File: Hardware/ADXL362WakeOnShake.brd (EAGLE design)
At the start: 43.2 x 24.1 mm, 25 parts, among them J1 PROG_HDR, U1 ADXL362, U3 ADP160-3.3

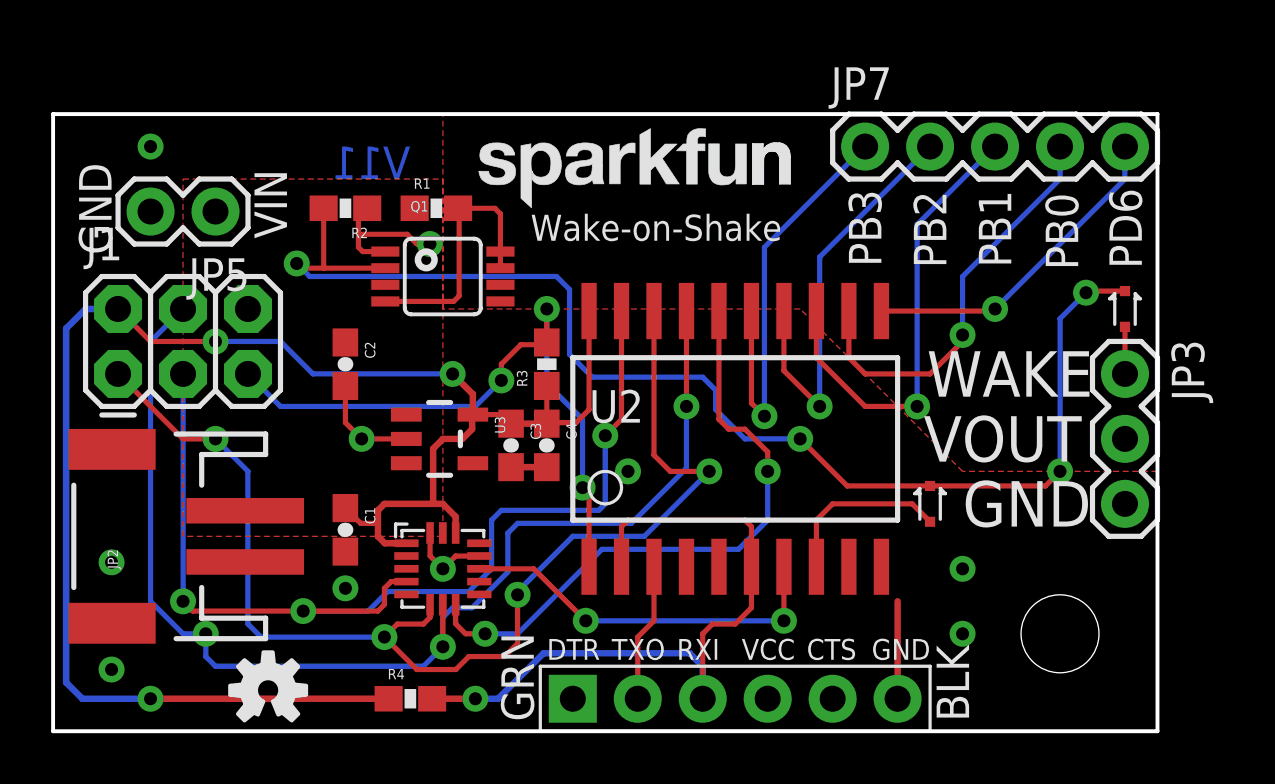
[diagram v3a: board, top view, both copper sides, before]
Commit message: added regular fiducials
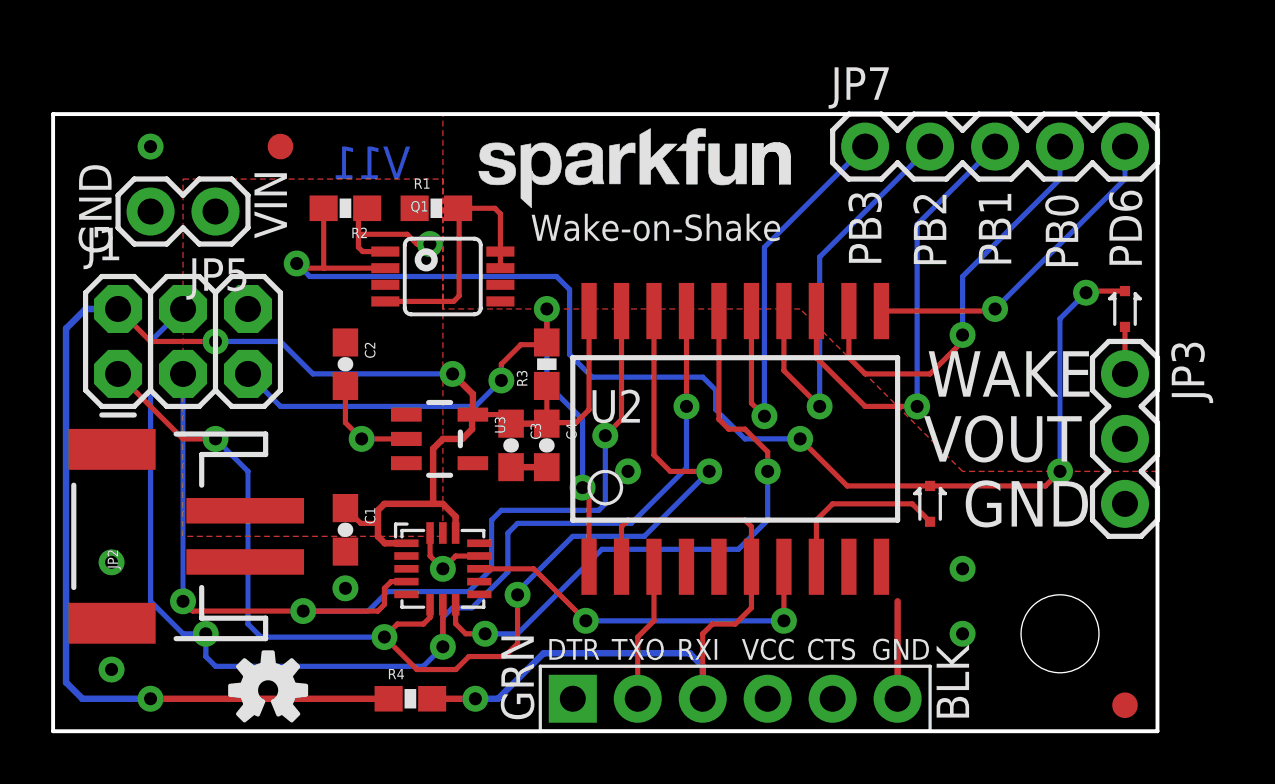
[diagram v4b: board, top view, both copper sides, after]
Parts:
- added FID1, FID2: FIDUCIAL1X2, SparkFun-Aesthetics:FIDUCIAL-1X2
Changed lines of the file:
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@@
 <?xml version="1.0" encoding="utf-8"?>
 <!DOCTYPE eagle SYSTEM "eagle.dtd">
-<eagle version="6.4">
+<eagle version="6.5.0">
 <drawing>
 <settings>
@@
 <setting verticaltext="up"/>
 </settings>
-<grid distance="0.05" unitdist="inch" unit="inch" style="lines" multiple="1" display="yes" altdistance="0.001" altunitdist="inch" altunit="inch"/>
+<grid distance="0.05" unitdist="inch" unit="inch" style="lines" multiple="1" display="yes" altdistance="0.01" altunitdist="inch" altunit="inch"/>
 <layers>
 <layer number="1" name="Top" color="4" fill="1" visible="yes" active="yes"/>
-<layer number="2" name="Route2" color="1" fill="3" visible="no" active="yes"/>
-<layer number="15" name="Route15" color="4" fill="6" visible="no" active="yes"/>
+<layer number="2" name="Route2" color="1" fill="3" visible="yes" active="yes"/>
+<layer number="15" name="Route15" color="4" fill="6" visible="yes" active="yes"/>
 <layer number="16" name="Bottom" color="1" fill="1" visible="yes" active="yes"/>
 <layer number="17" name="Pads" color="2" fill="1" visible="yes" active="yes"/>
 <layer number="18" name="Vias" color="2" fill="1" visible="yes" active="yes"/>
 <layer number="19" name="Unrouted" color="6" fill="1" visible="yes" active="yes"/>
-<layer number="20" name="Dimension" color="15" fill="1" visible="yes" active="yes"/>
-<layer number="21" name="tPlace" color="16" fill="1" visible="yes" active="yes"/>
-<layer number="22" name="bPlace" color="14" fill="1" visible="yes" active="yes"/>
+<layer number="20" name="Dimension" color="6" fill="1" visible="yes" active="yes"/>
+<layer number="21" name="tPlace" color="6" fill="1" visible="yes" active="yes"/>
+<layer number="22" name="bPlace" color="6" fill="1" visible="yes" active="yes"/>
 <layer number="23" name="tOrigins" color="15" fill="1" visible="yes" active="yes"/>
 <layer number="24" name="bOrigins" color="15" fill="1" visible="yes" active="yes"/>
-<layer number="25" name="tNames" color="7" fill="1" visible="no" active="yes"/>
-<layer number="26" name="bNames" color="7" fill="1" visible="no" active="yes"/>
-<layer number="27" name="tValues" color="7" fill="1" visible="no" active="yes"/>
-<layer number="28" name="bValues" color="7" fill="1" visible="no" active="yes"/>
-<layer number="29" name="tStop" color="7" fill="3" visible="no" active="yes"/>
-<layer number="30" name="bStop" color="7" fill="6" visible="no" active="yes"/>
-<layer number="31" name="tCream" color="7" fill="4" visible="no" active="yes"/>
-<layer number="32" name="bCream" color="7" fill="5" visible="no" active="yes"/>
-<layer number="39" name="tKeepout" color="4" fill="11" visible="no" active="yes"/>
-<layer number="40" name="bKeepout" color="1" fill="11" visible="no" active="yes"/>
-<layer number="41" name="tRestrict" color="4" fill="10" visible="no" active="yes"/>
-<layer number="42" name="bRestrict" color="1" fill="10" visible="no" active="yes"/>
-<layer number="44" name="Drills" color="7" fill="1" visible="no" active="yes"/>
+<layer number="25" name="tNames" color="7" fill="1" visible="yes" active="yes"/>
+<layer number="26" name="bNames" color="7" fill="1" visible="yes" active="yes"/>
+<layer number="27" name="tValues" color="7" fill="1" visible="yes" active="yes"/>
+<layer number="28" name="bValues" color="7" fill="1" visible="yes" active="yes"/>
+<layer number="29" name="tStop" color="7" fill="3" visible="yes" active="yes"/>
+<layer number="30" name="bStop" color="7" fill="6" visible="yes" active="yes"/>
+<layer number="31" name="tCream" color="7" fill="4" visible="yes" active="yes"/>
+<layer number="32" name="bCream" color="7" fill="5" visible="yes" active="yes"/>
+<layer number="39" name="tKeepout" color="4" fill="11" visible="yes" active="yes"/>
+<layer number="40" name="bKeepout" color="1" fill="11" visible="yes" active="yes"/>
+<layer number="41" name="tRestrict" color="4" fill="10" visible="yes" active="yes"/>
+<layer number="42" name="bRestrict" color="1" fill="10" visible="yes" active="yes"/>
+<layer number="44" name="Drills" color="7" fill="1" visible="yes" active="yes"/>
 <layer number="45" name="Holes" color="7" fill="1" visible="yes" active="yes"/>
-<layer number="46" name="Milling" color="3" fill="1" visible="no" active="yes"/>
+<layer number="46" name="Milling" color="3" fill="1" visible="yes" active="yes"/>
 <layer number="51" name="tDocu" color="6" fill="1" visible="yes" active="yes"/>
-<layer number="52" name="bDocu" color="7" fill="1" visible="no" active="yes"/>
+<layer number="52" name="bDocu" color="7" fill="1" visible="yes" active="yes"/>
 <layer number="3" name="Route3" color="4" fill="3" visible="no" active="no"/>
 <layer number="4" name="Route4" color="1" fill="4" visible="no" active="no"/>
@@
 <layer number="106" name="bPlate" color="7" fill="1" visible="no" active="no"/>
 <layer number="107" name="Crop" color="7" fill="1" visible="no" active="no"/>
-<layer number="108" name="tplace-old" color="10" fill="1" visible="no" active="yes"/>
-<layer number="109" name="ref-old" color="11" fill="1" visible="no" active="yes"/>
+<layer number="108" name="tplace-old" color="10" fill="1" visible="yes" active="yes"/>
+<layer number="109" name="ref-old" color="11" fill="1" visible="yes" active="yes"/>
 <layer number="116" name="Patch_BOT" color="9" fill="4" visible="no" active="no"/>
 <layer number="121" name="_tsilk" color="7" fill="1" visible="no" active="no"/>
@@
 <element name="U$4" library="Testing" package="STAND-OFF-TIGHT" value="" x="39.37" y="3.81"/>
 <element name="U$3" library="SparkFun-Aesthetics" package="OSHW-LOGO-S" value="" x="8.4074" y="1.6002"/>
+<element name="FID1" library="SparkFun-Aesthetics" package="FIDUCIAL-1X2" value="FIDUCIAL1X2" x="41.91" y="1.016"/>
+<element name="FID2" library="SparkFun-Aesthetics" package="FIDUCIAL-1X2" value="FIDUCIAL1X2" x="8.89" y="22.86"/>
 </elements>
 <signals>
